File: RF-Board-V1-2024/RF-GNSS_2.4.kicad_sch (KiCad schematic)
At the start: 10 parts, among them J4 UART, J5 Conn_Coaxial, U5 MAX-M10S

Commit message: i think schematic is done for now
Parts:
- added J7: Conn_Coaxial, footprints:TAOGLAS_EMPCB.SMAFSTJ.B.HT, symbol Connector:Conn_Coaxial
- renumbered U5 to RF1
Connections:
- net GND: now also J7.2 (Ext)
- net at RF2.1 (ANT): now also J7.1 (In)
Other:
- note added: "VG2392S240X0M2 2.4GHz LoRa"
- title: (none) -> RF GNSS 2.4GHz
- moved on the sheet: C12, RF2

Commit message: sd card need to do gnss
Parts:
- added C18: 10u, symbol Device:C
- added C31, C32: 100u, Capacitor_SMD:CP_Elec_6.3x5.9, symbol Device:C_Polarized
- added C33, C34, C35: 100nF, symbol Device:C
- added D11, D9: LED, LED_SMD:LED_0603_1608Metric, symbol Device:LED
- added R11, R13: 2k2, Resistor_SMD:R_0603_1608Metric, symbol Device:R
- added R18, R20: 140R, Resistor_SMD:R_0603_1608Metric, symbol Device:R
- C12: value 100nF -> 10u
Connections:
- net +3.3V: now also C18.2, C31.1, C32.1, C33.2, C34.2, C35.2, R11.1, R13.1
- net 24.NSS: now also D11.2 (A)
- net GND: now also C18.1, C31.2, C32.2, C33.1, C34.1, C35.1, R18.2, R20.2
- net GNSS.I2CSCL: now also R13.2
- net GNSS.I2CSDA: now also R11.2
- net GNSS.RST renamed ~{GNSS.RST}
- new net: D9.1 (K), R18.1
- new net: D11.1 (K), R20.1
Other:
- moved on the sheet: J4, J5, J7, RF1, RF2, TP1, TP2, TP3, TP4

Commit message: i think GNSS is done and micro sd are done
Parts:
- added BT1: 6.8MM_COIN_CELL, symbol Device:Battery_Cell
- added C42: 1u, symbol Device:C
- added D7: 0.5A/40V/420mV, Diode_SMD:D_SOD-123, symbol Device:D_Schottky
- added R16: 3k3, symbol Device:R
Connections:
- net +3.3V: now also D7.2 (A); no longer RF1.6 (V_BCKP)
- net GND: now also BT1.2 (-), C42.2
- net TP: now reaches RF1.4 (TIMEPULSE), TP1.1
- net TP: now also D9.2 (A)
- new net: D7.1 (K), R16.1
- new net BACKUP: BT1.1 (+), C42.1, R16.2, RF1.6 (V_BCKP)
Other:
- moved on the sheet: TP1

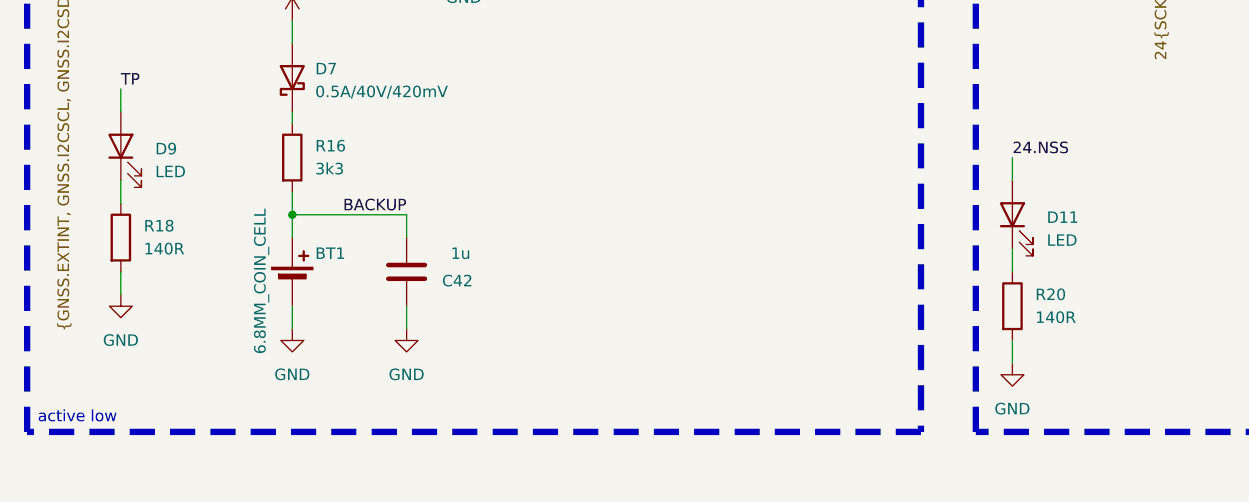
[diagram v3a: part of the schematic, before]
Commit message: changed the led resistors to 1k
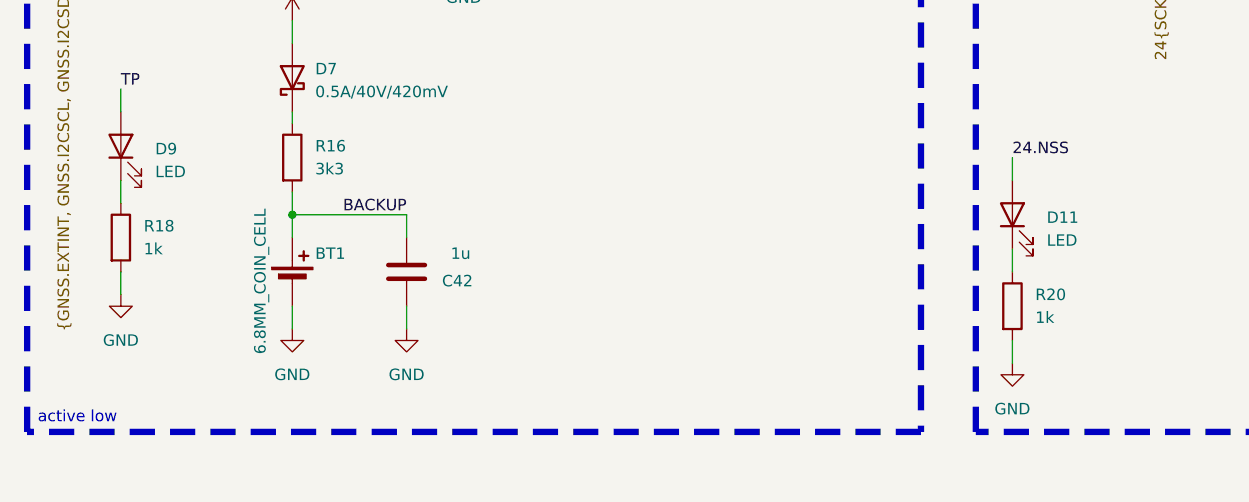
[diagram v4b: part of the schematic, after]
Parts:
- R18, R20: value 140R -> 1k
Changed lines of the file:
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@@
 			)
 		)
-		(property "Value" "140R"
+		(property "Value" "1k"
 			(at 27.94 119.3799 0)
 			(effects
@@
 			)
 		)
-		(property "Value" "140R"
+		(property "Value" "1k"
 			(at 127 126.9999 0)
 			(effects

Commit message: schematic done
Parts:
- removed D11: LED, LED_SMD:LED_0603_1608Metric, symbol Device:LED
- removed J5, J7: Conn_Coaxial, footprints:TAOGLAS_EMPCB.SMAFSTJ.B.HT, symbol Connector:Conn_Coaxial
- removed R20: 1k, Resistor_SMD:R_0603_1608Metric, symbol Device:R
- added D8: LED, LED_SMD:LED_0603_1608Metric, symbol Device:LED
- added J5: RFPC-SMA28-F, ecocad_lib_footprints:GRADCONN_RFPC-SMA28-F, symbol ecocad_lib_symbols:RFPC-SMA28-F
- added J6: RFPC-SMA29-F, ecocad_lib_footprints:GRADCONN_RFPC-SMA29-F, symbol ecocad_lib_symbols:RFPC-SMA29-F
- added R17: 600, Resistor_SMD:R_0603_1608Metric, symbol Device:R
- R18: value 1k -> 600
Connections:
- net 24.NSS: now also R18.1
- net GND: now also D9.1 (K), D8.1 (K), J5.G1, J5.G2, J5.G3, J5.G4, J6.G1, J6.G2, J6.G3, J6.G4; no longer R18.2
- net TP: now also R17.1; no longer D9.2 (A)
- net at RF2.1 (ANT): now also J6.1
- net at RF1.11 (RF_IN): now also J5.1
- new net: D8.2 (A), R17.2
- new net: D9.2 (A), R18.2

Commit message: basic layout done
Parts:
- removed BT1: 6.8MM_COIN_CELL, symbol Device:Battery_Cell
- added BT1: 3034TR, ecocad_lib_footprints:BAT_3034TR, symbol ecocad_lib_symbols:3034TR
- added C43, C44: 100n, Capacitor_SMD:C_0805_2012Metric, symbol Device:C
- added R26, R27: 10k, Resistor_SMD:R_0805_2012Metric, symbol Device:R
- added SW4, SW5: SW_SPST, Button_Switch_SMD:SW_DIP_SPSTx01_Slide_6.7x4.1mm_W6.73mm_P2.54mm_LowProfile_JPin, symbol Switch:SW_SPST
- C12, C18, C42: footprint (none) -> Capacitor_SMD:C_0805_2012Metric
- C20, C33, C34, C35: value 100nF -> 100n; footprint (none) -> Capacitor_SMD:C_0805_2012Metric
- D8, D9: footprint LED_SMD:LED_0603_1608Metric -> LED_SMD:LED_0805_2012Metric
- J4: footprint (none) -> Connector_PinHeader_2.54mm:PinHeader_1x02_P2.54mm_Vertical
- R11, R13, R17, R18: footprint Resistor_SMD:R_0603_1608Metric -> Resistor_SMD:R_0805_2012Metric
- R16: footprint (none) -> Resistor_SMD:R_0805_2012Metric
- RF2: footprint (none) -> ecocad_lib_footprints:Vollgo VG2392S240X0M2
- TP1, TP2, TP3, TP4: footprint (none) -> TestPoint:TestPoint_Pad_2.0x2.0mm
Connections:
- net +3.3V: now also R26.1, R27.1
- net 24.RST: now also C44.1, R27.2, SW5.2 (B)
- net BACKUP: now also BT1.P1
- net GND: now also BT1.N, C43.2, C44.2, SW4.1 (A), SW5.1 (A)
- net ~{GNSS.RST}: now also C43.1, R26.2, SW4.2 (B)
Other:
- moved on the sheet: C42

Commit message: idk what this is
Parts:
- RF1: DK # (none) -> 672-MAX-M10S-00BCT-ND
- RF2: LCSC # (none) -> C2976523
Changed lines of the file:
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@@
+			)
+		)
+		(property "DK #" "672-MAX-M10S-00BCT-ND"
+			(at 63.5 64.77 0)
+			(effects
+				(font
+					(size 1.27 1.27)
+				)
+				(hide yes)
 			)
 		)
@@
 			(at 166.37 60.96 0)
 			(effects
+				(font
+					(size 1.27 1.27)
+				)
+				(hide yes)
+			)
+		)
+		(property "LCSC #" "C2976523"
+			(at 166.37 60.96 0)
+			(effects

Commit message: cyhanged buttons
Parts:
- SW4, SW5: footprint Button_Switch_SMD:SW_DIP_SPSTx01_Slide_6.7x4.1mm_W6.73mm_P2.54mm_LowProfile_JPin -> Button_Switch_THT:SW_PUSH_6mm
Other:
- company: (none) -> University Of Alberta EcoCar Team
- title: RF GNSS 2.4GHz -> UltraCom Telemetry
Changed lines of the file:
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@@
 	(paper "A4")
 	(title_block
-		(title "RF GNSS 2.4GHz")
+		(title "UltraCom Telemetry")
+		(rev "Series. 1")
+		(company "University Of Alberta EcoCar Team")
 	)
 	(junction
@@
 			)
 		)
-		(property "Footprint" "Button_Switch_SMD:SW_DIP_SPSTx01_Slide_6.7x4.1mm_W6.73mm_P2.54mm_LowProfile_JPin"
+		(property "Footprint" "Button_Switch_THT:SW_PUSH_6mm"
 			(at 223.52 119.38 0)
 			(effects
@@
 			)
 		)
-		(property "Footprint" "Button_Switch_SMD:SW_DIP_SPSTx01_Slide_6.7x4.1mm_W6.73mm_P2.54mm_LowProfile_JPin"
+		(property "Footprint" "Button_Switch_THT:SW_PUSH_6mm"
 			(at 88.9 132.08 0)
 			(effects
